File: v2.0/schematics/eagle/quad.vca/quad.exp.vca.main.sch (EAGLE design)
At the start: 79 parts, among them IC1 TL084P, IC2 LM13700N, IC4 LM13700N, J1 CV1, J10 IN4, J11 OUT4, J12 CV4, J2 IN3, J3 IN1, J4 OUT1, J5 CV2, J6 OUT3, J7 IN2, J8 OUT2, J9 CV3, Q1 2N3904, Q2 2N3906, Q3 2N3904, Q4 2N3906, Q5 2N3906, Q6 2N3904, Q7 2N3906, Q8 2N3904

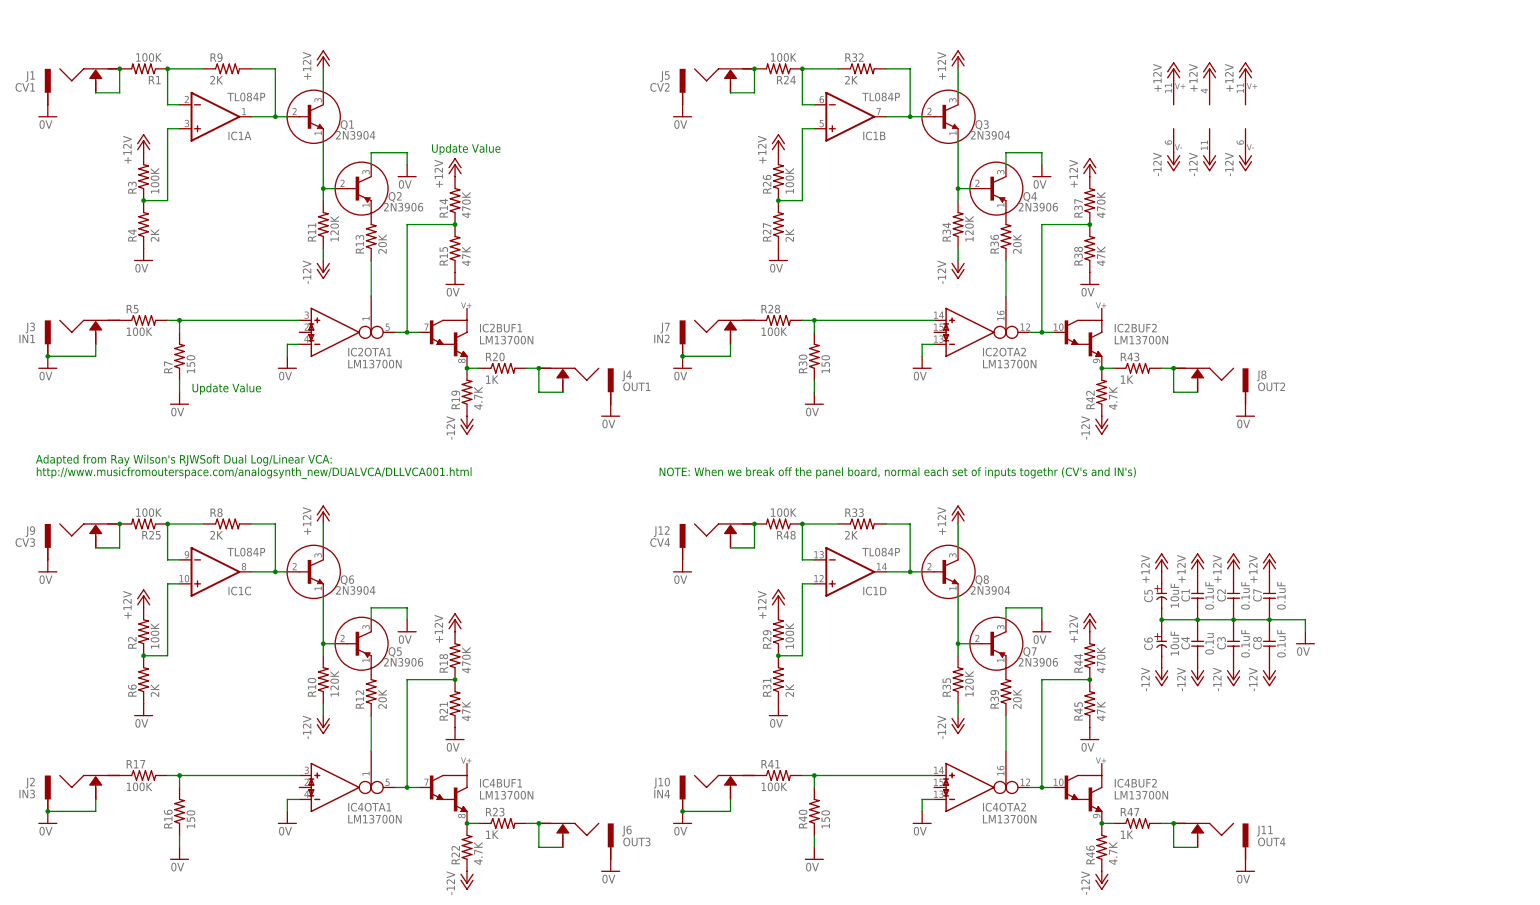
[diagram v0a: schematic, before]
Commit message: Replaced trim pots with tested fixed values. Corrected error in PNP transisitor connection
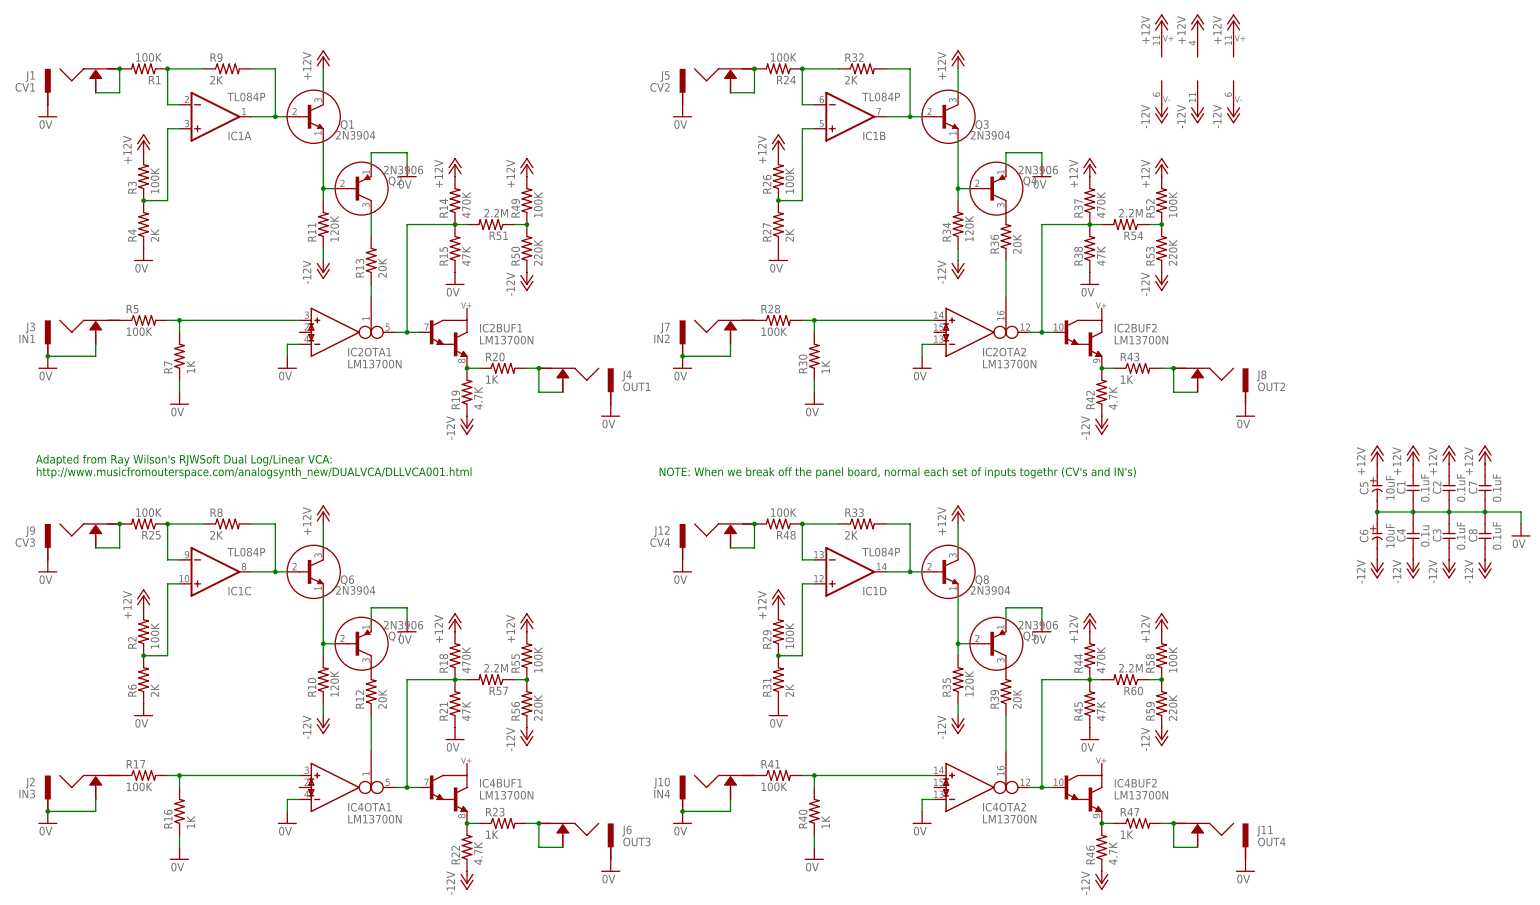
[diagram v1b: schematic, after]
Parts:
- added R49, R52, R55, R58: 100K, resistor:R-US_0207/7
- added R50, R53, R56, R59: 220K, resistor:R-US_0207/7
- added R51, R54, R57, R60: 2.2M, resistor:R-US_0207/7
- R16, R30, R40, R7: value 150 -> 1K
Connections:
- new net N$49: R49.1, R50.2, R51.1
- new net N$50: R52.1, R53.2, R54.1
- new net N$51: R55.1, R56.2, R57.1
- new net N$52: R58.1, R59.2, R60.1
- net +12V: now also R49.2, R52.2, R55.2, R58.2
- net -12V: now also R50.1, R53.1, R56.1, R59.1
- net 0V: now also Q2.E, Q4.E, Q5.E, Q7.E; no longer Q2.C, Q4.C, Q5.C, Q7.C
- net N$14: now also Q7.B; no longer Q5.B
- net N$15: now also R51.2
- net N$17: now also Q4.C, R36.2; no longer Q5.E, R12.2
- net N$20: now also R57.2
- net N$30: now also Q5.C, R39.2; no longer Q4.E, R36.2
- net N$35: now also R54.2
- net N$40: now also Q5.B; no longer Q7.B
- net N$41: now also Q7.C, R12.2; no longer Q7.E, R39.2
- net N$45: now also R60.2
- net N$9: now also Q2.C; no longer Q2.E
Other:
- note removed: "Update Value"
- moved on the sheet: C1, C2, C3, C4, C5, C6, C7, C8, Q2, Q4, Q5, Q7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

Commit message: renumber parts
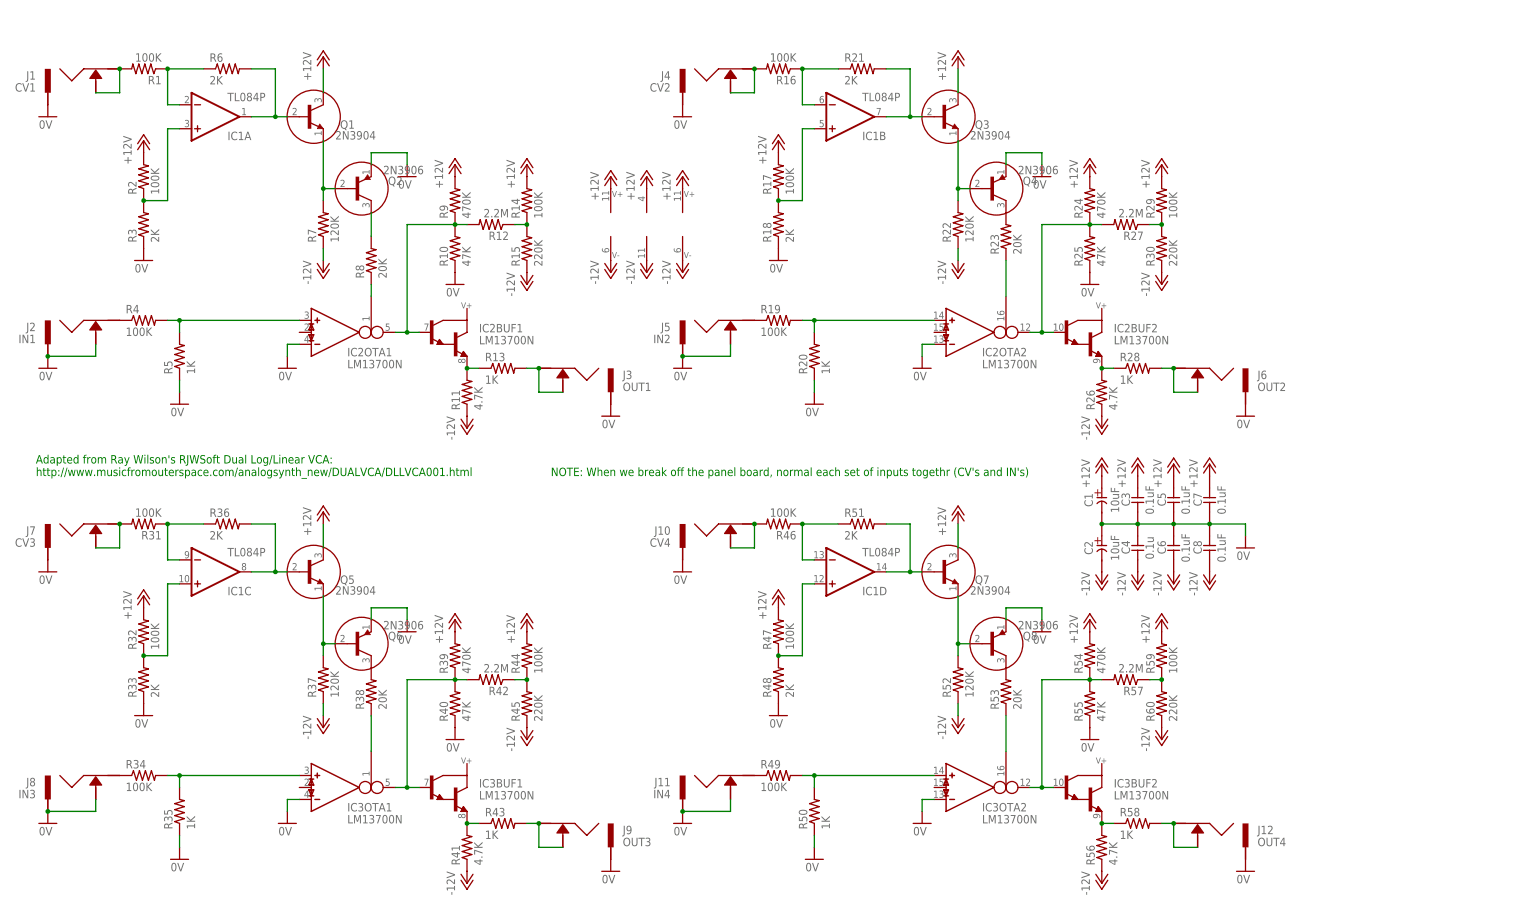
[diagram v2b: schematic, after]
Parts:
- C1, C2: value 0.1uF -> 10uF; device _common:CC-US025-024X044 -> _common:CE-USE2-5
- C5, C6: value 10uF -> 0.1uF; device _common:CE-USE2-5 -> _common:CC-US025-024X044
- J10: value IN4 -> CV4
- J11: value OUT4 -> IN4
- J12: value CV4 -> OUT4
- J2: value IN3 -> IN1
- J3: value IN1 -> OUT1
- J4: value OUT1 -> CV2
- J5: value CV2 -> IN2
- J6: value OUT3 -> OUT2
- J7: value IN2 -> CV3
- J8: value OUT2 -> IN3
- J9: value CV3 -> OUT3
- Q5, Q7: value 2N3906 -> 2N3904; device _common:2N3906 -> _common:2N3904
- Q6, Q8: value 2N3904 -> 2N3906; device _common:2N3904 -> _common:2N3906
- R10: value 120K -> 47K
- R11: value 120K -> 4.7K
- R12: value 20K -> 2.2M
- R13: value 20K -> 1K
- R14, R44: value 470K -> 100K
- R15, R45: value 47K -> 220K
- R16, R47: value 1K -> 100K
- R18: value 470K -> 2K
- R19, R46: value 4.7K -> 100K
- R21: value 47K -> 2K
- R22: value 4.7K -> 120K
- R23: value 1K -> 20K
- R24: value 100K -> 470K
- R25, R55: value 100K -> 47K
- R26, R41: value 100K -> 4.7K
- R27: value 2K -> 2.2M
- R28, R5, R58: value 100K -> 1K
- R3, R48: value 100K -> 2K
- R30: value 1K -> 220K
- R31, R32, R4: value 2K -> 100K
- R34: value 120K -> 100K
- R35: value 120K -> 1K
- R36: value 20K -> 2K
- R37: value 470K -> 120K
- R38: value 47K -> 20K
- R39: value 20K -> 470K
- R40: value 1K -> 47K
- R42: value 4.7K -> 2.2M
- R50: value 220K -> 1K
- R51: value 2.2M -> 2K
- R52: value 100K -> 120K
- R53: value 220K -> 20K
- R54: value 2.2M -> 470K
- R56: value 220K -> 4.7K
- R59: value 220K -> 100K
- R60: value 2.2M -> 220K
- R7: value 1K -> 120K
- R8: value 2K -> 20K
- R9: value 2K -> 470K
- renumbered IC4 to IC3
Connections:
- net +12V: now also C1.+, C3.1, C5.1, Q5.C, Q7.C, R17.2, R24.2, R32.2, R39.2, R47.2, R54.2, R59.2, R9.2; no longer C1.1, C2.1, C5.+, Q6.C, Q8.C, R18.2, R26.2, R3.2, R37.2, R49.2, R52.2, R55.2, R58.2
- net -12V: now also C2.-, C6.2, R15.1, R26.1, R30.1, R37.1, R41.1, R45.1, R52.1, R60.1, R7.1; no longer C3.2, C6.-, R10.1, R19.1, R34.1, R35.1, R42.1, R46.1, R50.1, R53.1, R59.1
- net 0V: now also C1.-, C2.+, C3.2, C5.2, C6.1, J11.P$3, J5.P$3, J8.P$3, Q6.E, Q8.E, R10.1, R18.1, R20.1, R25.1, R3.1, R33.1, R35.1, R48.1, R5.1, R50.1, R55.1; no longer C1.2, C2.2, C3.1, C5.-, C6.+, J10.P$3, J3.P$3, J7.P$3, Q5.E, Q7.E, R15.1, R16.1, R21.1, R27.1, R30.1, R31.1, R38.1, R4.1, R45.1, R6.1, R7.1
- net N$1: now also J9.P$2, J9.P$3, R43.2; no longer J6.P$2, J6.P$3, R23.2
- net N$10: now also Q5.B, R36.2; no longer Q6.B, R8.2
- net N$11: now also J2.P$2, R4.1; no longer J3.P$2, R5.1
- net N$12: now also R4.2; no longer R7.2
- net N$13: now also R11.2, R13.1; no longer R19.2, R20.1
- net N$14: now also Q5.E, Q6.B, R37.2; no longer Q6.E, Q7.B, R10.2
- net N$15: now also R10.2, R12.2, R9.1; no longer R14.1, R15.2, R51.2
- net N$17: now also R23.2; no longer R36.2
- net N$18: now also J8.P$2, R34.1; no longer J2.P$2, R17.1
- net N$19: now also R34.2, R35.2; no longer R16.2, R17.2
- net N$2: now also J3.P$2, J3.P$3, R13.2; no longer J4.P$2, J4.P$3, R20.2
- net N$20: now also R39.1, R40.2, R42.2; no longer R18.1, R21.2, R57.2
- net N$21: now also R8.1; no longer R13.1
- net N$22: now also R41.2, R43.1; no longer R22.2, R23.1
- net N$23: now also J7.P$2, J7.P$3, R31.2; no longer J9.P$2, J9.P$3, R25.2
- net N$24: now also J6.P$2, J6.P$3, R28.2; no longer J8.P$2, J8.P$3, R43.2
- net N$25: now also R17.1, R18.2; no longer R26.1, R27.2
- net N$26: now also R16.1, R21.1; no longer R24.1, R32.1
- net N$27: now also R38.1; no longer R12.1
- net N$28: now also R21.2; no longer R32.2
- net N$29: now also R22.2; no longer R34.2
- net N$3: now also R2.1, R3.2; no longer R3.1, R4.2
- net N$30: now also Q8.C, R53.2; no longer Q5.C, R39.2
- net N$31: now also J12.P$2, J12.P$3, R58.2; no longer J11.P$2, J11.P$3, R47.2
- net N$32: now also J5.P$2, R19.1; no longer J7.P$2, R28.1
- net N$33: now also R19.2, R20.2; no longer R28.2, R30.2
- net N$34: now also R47.1, R48.2; no longer R29.1, R31.2
- net N$35: now also R24.1, R25.2, R27.2; no longer R37.1, R38.2, R54.2
- net N$36: now also R26.2, R28.1; no longer R42.2, R43.1
- net N$37: now also J4.P$2, J4.P$3, R16.2; no longer J5.P$2, J5.P$3, R24.2
- net N$38: now also R46.1, R51.1; no longer R33.1, R48.1
- net N$39: now also Q7.B, R51.2; no longer Q8.B, R33.2
- net N$4: now also R6.1; no longer R9.1
- net N$40: now also Q7.E, Q8.B, R52.2; no longer Q5.B, Q8.E, R35.2
- net N$41: now also Q6.C, R38.2; no longer Q7.C, R12.2
- net N$42: now also J11.P$2, R49.1; no longer J10.P$2, R41.1
- net N$43: now also R49.2, R50.2; no longer R40.2, R41.2
- net N$44: now also R23.1; no longer R36.1
- net N$45: now also R54.1, R55.2, R57.2; no longer R44.1, R45.2, R60.2
- net N$46: now also R56.2, R58.1; no longer R46.2, R47.1
- net N$47: now also J10.P$2, J10.P$3, R46.2; no longer J12.P$2, J12.P$3, R48.2
- net N$48: now also R53.1; no longer R39.1
- net N$49: now also R12.1, R14.1, R15.2; no longer R49.1, R50.2, R51.1
- net N$5: now also R32.1, R33.2; no longer R2.1, R6.2
- net N$50: now also R27.1, R29.1, R30.2; no longer R52.1, R53.2, R54.1
- net N$51: now also R42.1, R44.1, R45.2; no longer R55.1, R56.2, R57.1
- net N$52: now also R57.1, R59.1, R60.2; no longer R58.1, R59.2, R60.1
- net N$6: now also R6.2; no longer R9.2
- net N$7: now also R7.2; no longer R11.2
- net N$8: now also R31.1, R36.1; no longer R25.1, R8.1
- net N$9: now also R8.2; no longer R13.2
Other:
- moved on the sheet: C1, C2, C3, C4, C5, C6, C7, C8, J10, J11, J12, J2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
